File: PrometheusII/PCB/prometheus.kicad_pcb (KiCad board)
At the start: 4 copper layers, 223.5 x 222.3 mm, 203 parts, among them J1 0878311420, J10 Conn_02x02_Odd_Even, J11 Conn_02x02_Odd_Even, J16 Conn_02x07_Odd_Even, J17 Conn_02x07_Odd_Even, J18 Conn_02x07_Odd_Even, J19 Conn_02x07_Odd_Even, J2 Conn_02x08_Odd_Even, J3 Conn_02x02_Odd_Even, J4 Conn_02x02_Odd_Even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

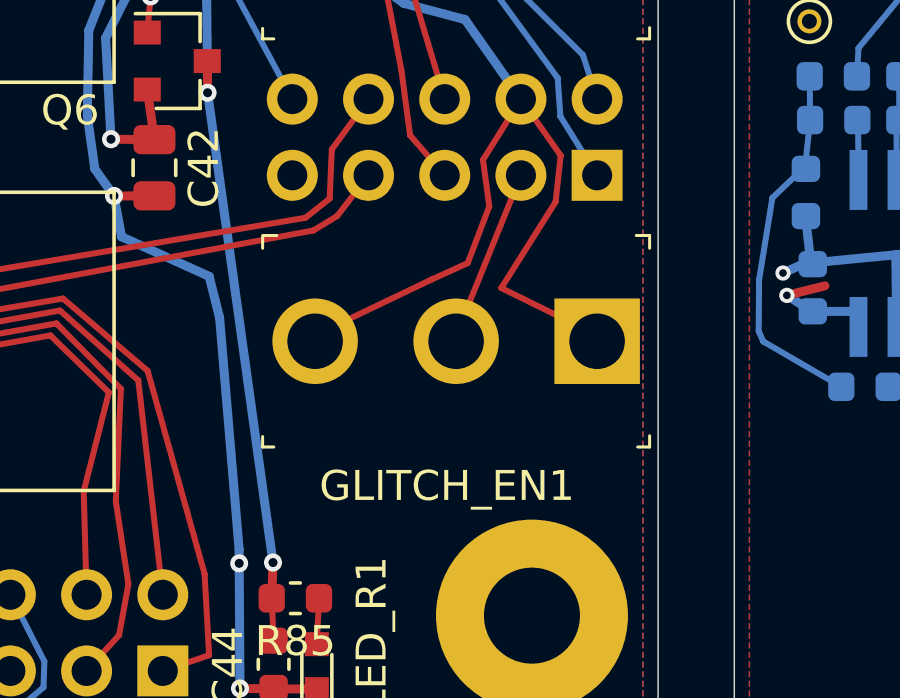
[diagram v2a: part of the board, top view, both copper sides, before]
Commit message: Changed switch PN, keeping footprint the same for now
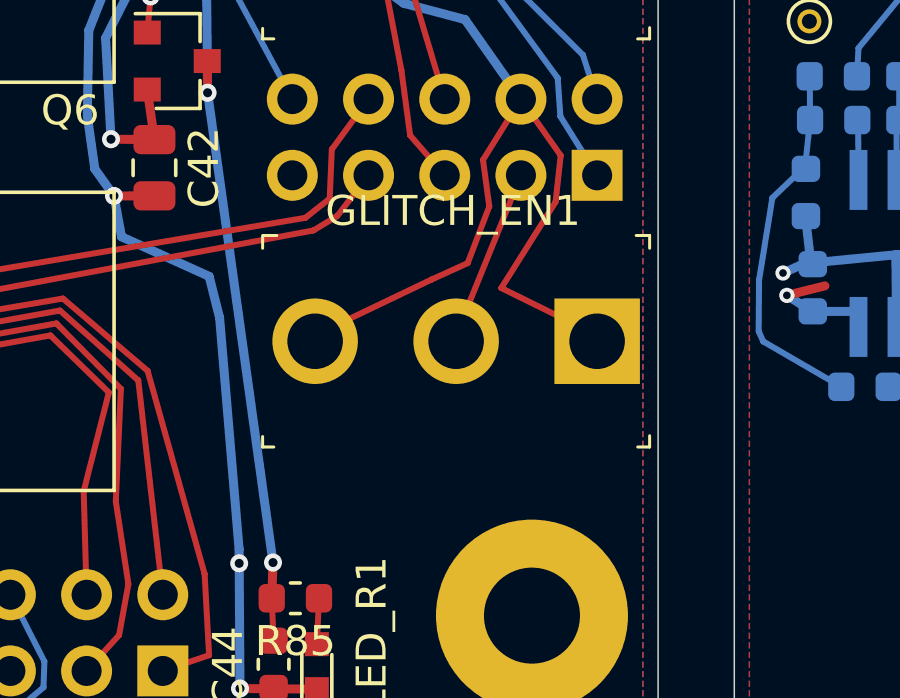
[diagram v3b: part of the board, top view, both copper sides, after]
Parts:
- FREQ_LOCK1, GLITCH_EN1: value 100SP5T1B1M2QEH -> TSM113F1; footprint digikey-footprints:Toggle_Switch_100SP1T1B4M2QE -> ttt_lib:Toggle_Switch_TSM113F1
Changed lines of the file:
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@@
     (add_net "Net-(U9-Pad1)")
   )
+  (module ttt_lib:Toggle_Switch_TSM113F1 locked (layer F.Cu)
+    (at 124.968 116.02 180)
+    (descr http://spec_sheets.e-switch.com/specs/T111597.pdf)
+    (fp_text reference GLITCH_EN1 (at 4.8045 4.34 180) (layer F.SilkS)
+      (effects (font (size 1 1) (thickness 0.15)))
+    )
+    (fp_text value TSM113F1 (at 4.65 4.82 180) (layer F.Fab)
+      (effects (font (size 1 1) (thickness 0.15)))
+    )
+    (fp_circle (center 4.7 0) (end 4.7 3.4) (layer F.Fab) (width 0.1))
+    (fp_line (start 11.3 -3.68) (end 11.3 3.68) (layer F.CrtYd) (width 0.05))
+    (fp_line (start 11.3 3.68) (end -1.9 3.68) (layer F.CrtYd) (width 0.05))
+    (fp_line (start -1.9 3.68) (end -1.9 -3.68) (layer F.CrtYd) (width 0.05))
+    (fp_line (start -1.9 -3.68) (end 11.3 -3.68) (layer F.CrtYd) (width 0.05))
+    (fp_text user %R (at 4.7 0 180) (layer F.Fab)
+      (effects (font (size 1 1) (thickness 0.15)))
+    )
+    (fp_line (start 11.15 3.525) (end 11.15 3.1) (layer F.SilkS) (width 0.1))
+    (fp_line (start 11.125 3.525) (end 10.675 3.525) (layer F.SilkS) (width 0.1))
+    (fp_line (start -1.75 3.525) (end -1.3 3.525) (layer F.SilkS) (width 0.1))
+    (fp_line (start -1.75 3.525) (end -1.75 3.1) (layer F.SilkS) (width 0.1))
+    (fp_line (start -1.75 -3.525) (end -1.75 -3.15) (layer F.SilkS) (width 0.1))
+    (fp_line (start -1.75 -3.525) (end -1.35 -3.525) (layer F.SilkS) (width 0.1))
+    (fp_line (start 10.775 -3.525) (end 11.15 -3.525) (layer F.SilkS) (width 0.1))
+    (fp_line (start 11.15 -3.525) (end 11.15 -3.175) (layer F.SilkS) (width 0.1))
+    (fp_line (start 11.05 3.43) (end 11.05 -3.43) (layer F.Fab) (width 0.1))
+    (fp_line (start -1.65 -3.43) (end -1.65 3.43) (layer F.Fab) (width 0.1))
+    (fp_line (start -1.65 3.43) (end 11.05 3.43) (layer F.Fab) (width 0.1))
+    (fp_line (start -1.65 -3.43) (end 11.05 -3.43) (layer F.Fab) (width 0.1))
+    (pad 1 thru_hole rect (at 0 0 180) (size 2.85 2.85) (drill 1.85) (layers *.Cu *.Mask)
+      (net 1 GND))
+    (pad 2 thru_hole circle (at 4.7 0 180) (size 2.85 2.85) (drill 1.85) (layers *.Cu *.Mask)
+      (net 85 /GLITCH_EN_P))
+    (pad 3 thru_hole circle (at 9.4 0 180) (size 2.85 2.85) (drill 1.85) (layers *.Cu *.Mask)
+      (net 1 GND))
+  )
+  (module ttt_lib:Toggle_Switch_TSM113F1 locked (layer F.Cu)
+    (at 124.968 102.416 180)
+    (descr http://spec_sheets.e-switch.com/specs/T111597.pdf)
+    (fp_text reference FREQ_LOCK1 (at 4.8045 4.34 180) (layer F.SilkS)
+      (effects (font (size 1 1) (thickness 0.15)))
+    )
+    (fp_text value TSM113F1 (at 4.65 4.82 180) (layer F.Fab)
+      (effects (font (size 1 1) (thickness 0.15)))
+    )
+    (fp_circle (center 4.7 0) (end 4.7 3.4) (layer F.Fab) (width 0.1))
+    (fp_line (start 11.3 -3.68) (end 11.3 3.68) (layer F.CrtYd) (width 0.05))
+    (fp_line (start 11.3 3.68) (end -1.9 3.68) (layer F.CrtYd) (width 0.05))
+    (fp_line (start -1.9 3.68) (end -1.9 -3.68) (layer F.CrtYd) (width 0.05))
+    (fp_line (start -1.9 -3.68) (end 11.3 -3.68) (layer F.CrtYd) (width 0.05))
+    (fp_text user %R (at 4.7 0 180) (layer F.Fab)
+      (effects (font (size 1 1) (thickness 0.15)))
+    )
+    (fp_line (start 11.15 3.525) (end 11.15 3.1) (layer F.SilkS) (width 0.1))
+    (fp_line (start 11.125 3.525) (end 10.675 3.525) (layer F.SilkS) (width 0.1))
+    (fp_line (start -1.75 3.525) (end -1.3 3.525) (layer F.SilkS) (width 0.1))
+    (fp_line (start -1.75 3.525) (end -1.75 3.1) (layer F.SilkS) (width 0.1))
+    (fp_line (start -1.75 -3.525) (end -1.75 -3.15) (layer F.SilkS) (width 0.1))
+    (fp_line (start -1.75 -3.525) (end -1.35 -3.525) (layer F.SilkS) (width 0.1))
+    (fp_line (start 10.775 -3.525) (end 11.15 -3.525) (layer F.SilkS) (width 0.1))
+    (fp_line (start 11.15 -3.525) (end 11.15 -3.175) (layer F.SilkS) (width 0.1))
+    (fp_line (start 11.05 3.43) (end 11.05 -3.43) (layer F.Fab) (width 0.1))
+    (fp_line (start -1.65 -3.43) (end -1.65 3.43) (layer F.Fab) (width 0.1))
+    (fp_line (start -1.65 3.43) (end 11.05 3.43) (layer F.Fab) (width 0.1))
+    (fp_line (start -1.65 -3.43) (end 11.05 -3.43) (layer F.Fab) (width 0.1))
+    (pad 1 thru_hole rect (at 0 0 180) (size 2.85 2.85) (drill 1.85) (layers *.Cu *.Mask)
+      (net 1 GND))
+    (pad 2 thru_hole circle (at 4.7 0 180) (size 2.85 2.85) (drill 1.85) (layers *.Cu *.Mask)
+      (net 93 /FREQ_LOCK_P))
+    (pad 3 thru_hole circle (at 9.4 0 180) (size 2.85 2.85) (drill 1.85) (layers *.Cu *.Mask)
+      (net 1 GND))
+  )
   (module ttt_lib:Teensy40_outerpins locked (layer B.Cu)
     (at 190.8302 109.0676 90)
@@
     )
   )
-  (module digikey-footprints:Toggle_Switch_100SP1T1B4M2QE locked (layer F.Cu)
-    (at 124.968 102.416 180)
-    (descr http://spec_sheets.e-switch.com/specs/T111597.pdf)
-    (fp_text reference FREQ_LOCK1 (at 4.8045 4.34) (layer F.SilkS)
-      (effects (font (size 1 1) (thickness 0.15)))
-    )
-    (fp_text value 100SP5T1B1M2QEH (at 4.65 4.82) (layer F.Fab)
-      (effects (font (size 1 1) (thickness 0.15)))
-    )
-    (fp_line (start -1.65 -3.43) (end 11.05 -3.43) (layer F.Fab) (width 0.1))
-    (fp_line (start -1.65 3.43) (end 11.05 3.43) (layer F.Fab) (width 0.1))
-    (fp_line (start -1.65 -3.43) (end -1.65 3.43) (layer F.Fab) (width 0.1))
-    (fp_line (start 11.05 3.43) (end 11.05 -3.43) (layer F.Fab) (width 0.1))
-    (fp_line (start 11.15 -3.525) (end 11.15 -3.175) (layer F.SilkS) (width 0.1))
-    (fp_line (start 10.775 -3.525) (end 11.15 -3.525) (layer F.SilkS) (width 0.1))
-    (fp_line (start -1.75 -3.525) (end -1.35 -3.525) (layer F.SilkS) (width 0.1))
-    (fp_line (start -1.75 -3.525) (end -1.75 -3.15) (layer F.SilkS) (width 0.1))
-    (fp_line (start -1.75 3.525) (end -1.75 3.1) (layer F.SilkS) (width 0.1))
-    (fp_line (start -1.75 3.525) (end -1.3 3.525) (layer F.SilkS) (width 0.1))
-    (fp_line (start 11.125 3.525) (end 10.675 3.525) (layer F.SilkS) (width 0.1))
-    (fp_line (start 11.15 3.525) (end 11.15 3.1) (layer F.SilkS) (width 0.1))
-    (fp_text user %R (at 4.7 0) (layer F.Fab)
-      (effects (font (size 1 1) (thickness 0.15)))
-    )
-    (fp_line (start -1.9 -3.68) (end 11.3 -3.68) (layer F.CrtYd) (width 0.05))
-    (fp_line (start -1.9 3.68) (end -1.9 -3.68) (layer F.CrtYd) (width 0.05))
-    (fp_line (start 11.3 3.68) (end -1.9 3.68) (layer F.CrtYd) (width 0.05))
-    (fp_line (start 11.3 -3.68) (end 11.3 3.68) (layer F.CrtYd) (width 0.05))
-    (fp_circle (center 4.7 0) (end 4.7 3.4) (layer F.Fab) (width 0.1))
-    (pad 3 thru_hole circle (at 9.4 0 180) (size 2.85 2.85) (drill 1.85) (layers *.Cu *.Mask)
-      (net 1 GND))
-    (pad 2 thru_hole circle (at 4.7 0 180) (size 2.85 2.85) (drill 1.85) (layers *.Cu *.Mask)
-      (net 93 /FREQ_LOCK_P))
-    (pad 1 thru_hole rect (at 0 0 180) (size 2.85 2.85) (drill 1.85) (layers *.Cu *.Mask)
-      (net 1 GND))
-  )
-  (module digikey-footprints:Toggle_Switch_100SP1T1B4M2QE locked (layer F.Cu)
-    (at 124.968 116.02 180)
-    (descr http://spec_sheets.e-switch.com/specs/T111597.pdf)
-    (fp_text reference GLITCH_EN1 (at 5.0045 -4.826) (layer F.SilkS)
-      (effects (font (size 1 1) (thickness 0.15)))
-    )
-    (fp_text value 100SP5T1B1M2QEH (at 4.65 4.82) (layer F.Fab)
-      (effects (font (size 1 1) (thickness 0.15)))
-    )
-    (fp_line (start -1.65 -3.43) (end 11.05 -3.43) (layer F.Fab) (width 0.1))
-    (fp_line (start -1.65 3.43) (end 11.05 3.43) (layer F.Fab) (width 0.1))
-    (fp_line (start -1.65 -3.43) (end -1.65 3.43) (layer F.Fab) (width 0.1))
-    (fp_line (start 11.05 3.43) (end 11.05 -3.43) (layer F.Fab) (width 0.1))
-    (fp_line (start 11.15 -3.525) (end 11.15 -3.175) (layer F.SilkS) (width 0.1))
-    (fp_line (start 10.775 -3.525) (end 11.15 -3.525) (layer F.SilkS) (width 0.1))
-    (fp_line (start -1.75 -3.525) (end -1.35 -3.525) (layer F.SilkS) (width 0.1))
-    (fp_line (start -1.75 -3.525) (end -1.75 -3.15) (layer F.SilkS) (width 0.1))
-    (fp_line (start -1.75 3.525) (end -1.75 3.1) (layer F.SilkS) (width 0.1))
-    (fp_line (start -1.75 3.525) (end -1.3 3.525) (layer F.SilkS) (width 0.1))
-    (fp_line (start 11.125 3.525) (end 10.675 3.525) (layer F.SilkS) (width 0.1))
-    (fp_line (start 11.15 3.525) (end 11.15 3.1) (layer F.SilkS) (width 0.1))
-    (fp_text user %R (at 4.7 0) (layer F.Fab)
-      (effects (font (size 1 1) (thickness 0.15)))
-    )
-    (fp_line (start -1.9 -3.68) (end 11.3 -3.68) (layer F.CrtYd) (width 0.05))
-    (fp_line (start -1.9 3.68) (end -1.9 -3.68) (layer F.CrtYd) (width 0.05))
-    (fp_line (start 11.3 3.68) (end -1.9 3.68) (layer F.CrtYd) (width 0.05))
-    (fp_line (start 11.3 -3.68) (end 11.3 3.68) (layer F.CrtYd) (width 0.05))
-    (fp_circle (center 4.7 0) (end 4.7 3.4) (layer F.Fab) (width 0.1))
-    (pad 3 thru_hole circle (at 9.4 0 180) (size 2.85 2.85) (drill 1.85) (layers *.Cu *.Mask)
-      (net 1 GND))
-    (pad 2 thru_hole circle (at 4.7 0 180) (size 2.85 2.85) (drill 1.85) (layers *.Cu *.Mask)
-      (net 85 /GLITCH_EN_P))
-    (pad 1 thru_hole rect (at 0 0 180) (size 2.85 2.85) (drill 1.85) (layers *.Cu *.Mask)
-      (net 1 GND))
-  )
   (module Resistor_SMD:R_0603_1608Metric locked (layer B.Cu)

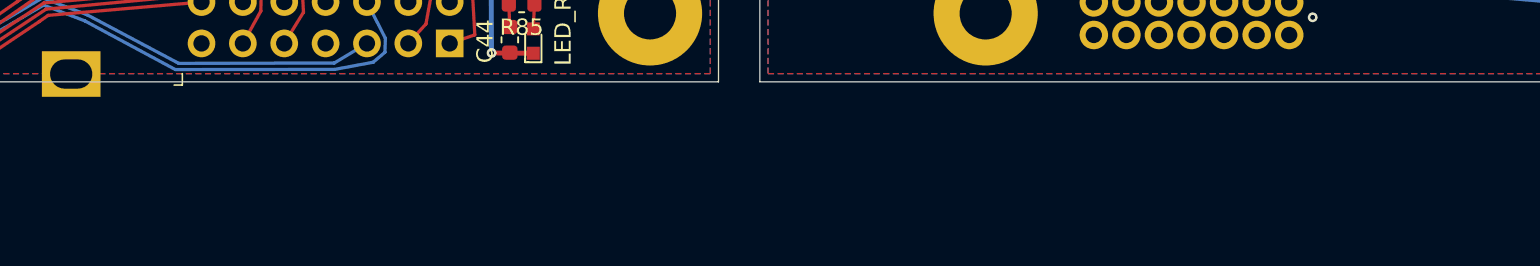
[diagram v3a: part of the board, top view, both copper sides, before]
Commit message: put fiducials in design
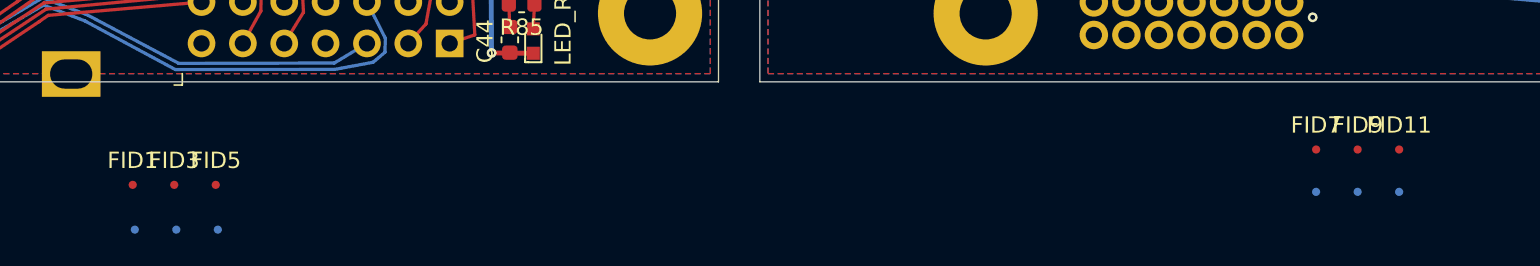
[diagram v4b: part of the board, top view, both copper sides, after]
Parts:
- added FID1: Fiducial, Fiducial:Fiducial_0.5mm_Mask1mm, F.Cu at (91.0, 135.7)
- added FID10: Fiducial, Fiducial:Fiducial_0.5mm_Mask1mm, B.Cu at (166.3, 136.1)
- added FID11: Fiducial, Fiducial:Fiducial_0.5mm_Mask1mm, F.Cu at (168.8, 133.5)
- added FID12: Fiducial, Fiducial:Fiducial_0.5mm_Mask1mm, B.Cu at (168.8, 136.1)
- added FID2: Fiducial, Fiducial:Fiducial_0.5mm_Mask1mm, B.Cu at (91.2, 138.4)
- added FID3: Fiducial, Fiducial:Fiducial_0.5mm_Mask1mm, F.Cu at (93.6, 135.7)
- added FID4: Fiducial, Fiducial:Fiducial_0.5mm_Mask1mm, B.Cu at (93.7, 138.4)
- added FID5: Fiducial, Fiducial:Fiducial_0.5mm_Mask1mm, F.Cu at (96.1, 135.7)
- added FID6: Fiducial, Fiducial:Fiducial_0.5mm_Mask1mm, B.Cu at (96.3, 138.4)
- added FID7: Fiducial, Fiducial:Fiducial_0.5mm_Mask1mm, F.Cu at (163.7, 133.5)
- added FID8: Fiducial, Fiducial:Fiducial_0.5mm_Mask1mm, B.Cu at (163.7, 136.1)
- added FID9: Fiducial, Fiducial:Fiducial_0.5mm_Mask1mm, F.Cu at (166.3, 133.5)

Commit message: Working on connector updates
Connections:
- U1 pad 20: /VOCT_FINE_T -> /FREQ_LOCK_T
- U1 pad 21: /VOCT_ATV_T -> /GLITCH_EN_T
- U1 pad 22: /VOCT_T -> /VOCT_FINE_T
- U1 pad 23: /PARAM_0_CV_T -> /VOCT_ATV_T
- U1 pad 24: /LFO_T -> /VOCT_T
- U1 pad 25: /LEN_CV_T -> /PARAM_0_CV_T
- U1 pad 26: /PARAM_0_T -> /LFO_T
- U1 pad 27: /PARAM_1_T -> /LEN_CV_T
- U1 pad 28: /LEN_KNOB_T -> /PARAM_0_T
- U1 pad 29: /FREQ_LOCK_T -> /PARAM_1_T
- U1 pad 30: /GLITCH_EN_T -> /LEN_KNOB_T

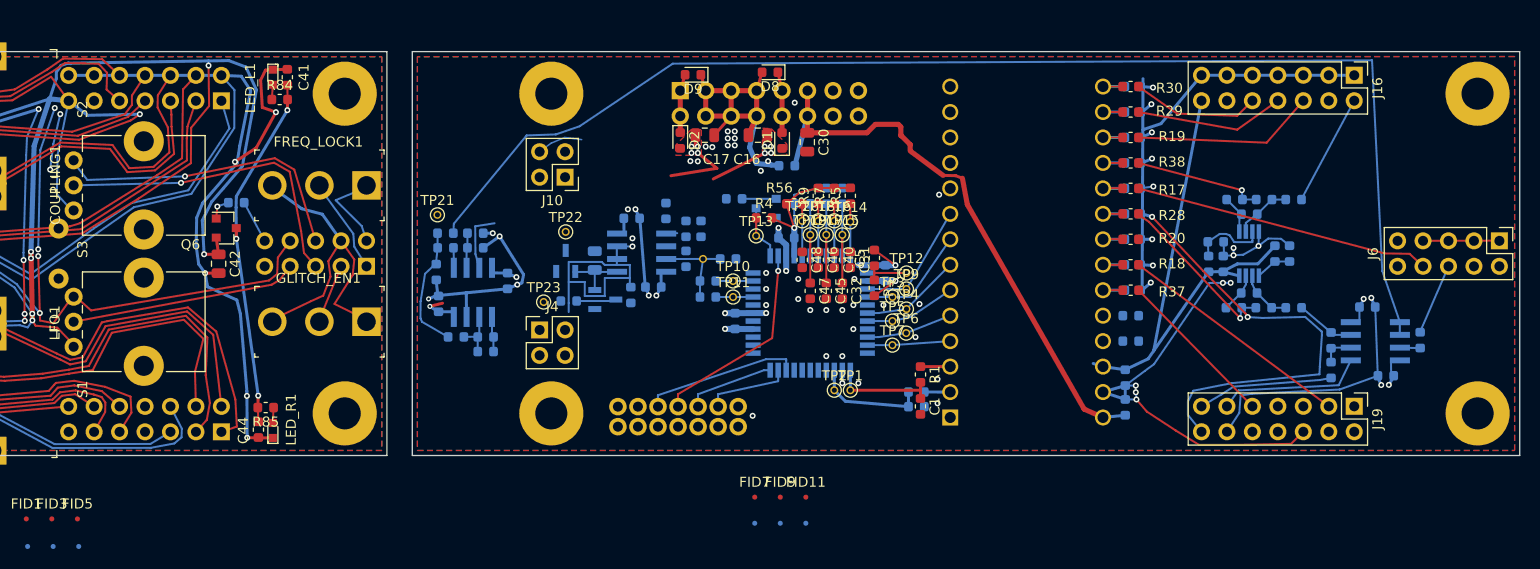
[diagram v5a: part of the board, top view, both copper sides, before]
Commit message: Updated connector placement and footprints
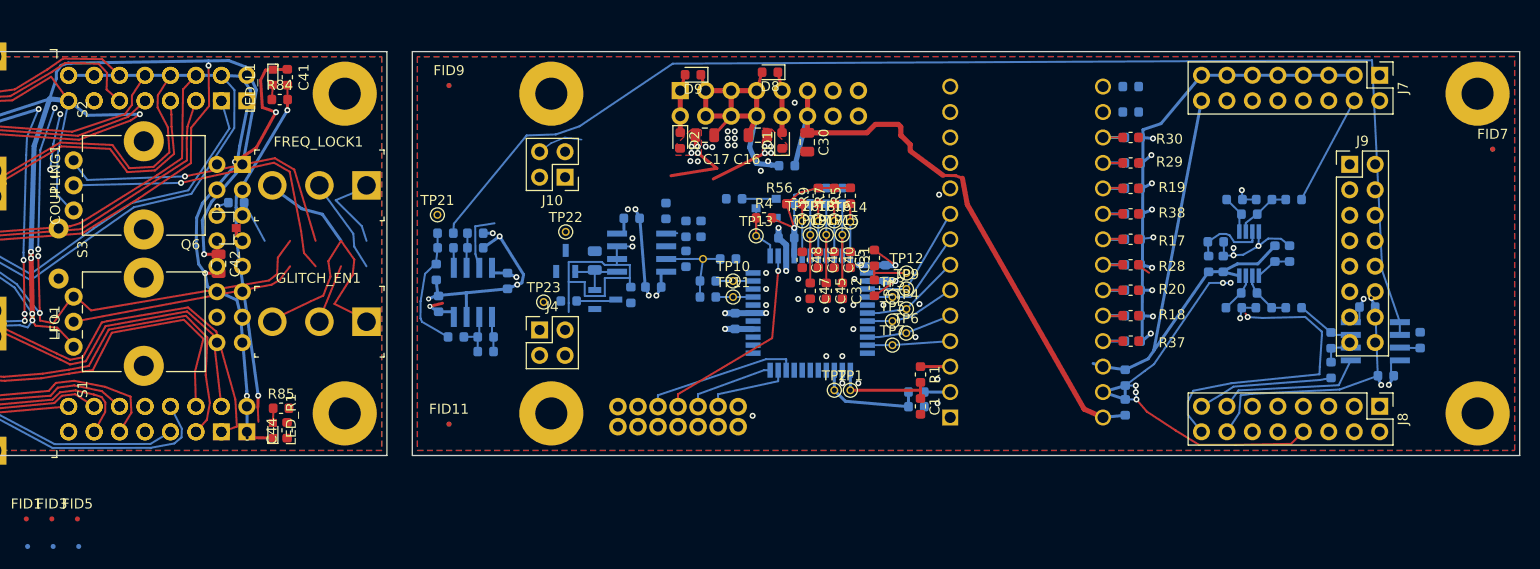
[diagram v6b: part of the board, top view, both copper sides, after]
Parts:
- removed J16, J19: Conn_02x07_Odd_Even, Connector_PinHeader_2.54mm:PinHeader_2x07_P2.54mm_Vertical
- removed J5, J6: Conn_02x05_Odd_Even, Connector_PinHeader_2.54mm:PinHeader_2x05_P2.54mm_Vertical
- added J12: Conn_02x08_Odd_Even, Connector_PinHeader_2.54mm:PinHeader_2x08_P2.54mm_Vertical, B.Cu at (112.6, 100.3)
- added J13: Conn_02x08_Odd_Even, Connector_PinHeader_2.54mm:PinHeader_2x08_P2.54mm_Vertical, B.Cu at (113.0, 94.0)
- added J14: Conn_02x08_Odd_Even, Connector_PinHeader_2.54mm:PinHeader_2x08_P2.54mm_Vertical, B.Cu at (113.0, 127.0)
- added J7: Conn_02x08_Odd_Even, Connector_PinHeader_2.54mm:PinHeader_2x08_P2.54mm_Vertical, F.Cu at (226.1, 91.4)
- added J8: Conn_02x08_Odd_Even, Connector_PinHeader_2.54mm:PinHeader_2x08_P2.54mm_Vertical, F.Cu at (226.1, 124.5)
- added J9: Conn_02x08_Odd_Even, Connector_PinHeader_2.54mm:PinHeader_2x08_P2.54mm_Vertical, F.Cu at (223.1, 100.3)
- moved FID8 82.6 mm to (237.3, 98.8)
- moved FID7 81.4 mm to (237.3, 98.8)
- moved FID10 54.8 mm to (133.2, 92.5)
- moved FID9 52.7 mm to (133.2, 92.5)
- moved FID12 37.0 mm to (133.2, 126.2)
- moved FID11 36.3 mm to (133.2, 126.2)
- moved R52 22.9 mm to (201.2, 92.6)
- moved R59 22.9 mm to (201.2, 95.1)
- moved C21 5.08 mm to (201.4, 97.6)
- moved R30 5.08 mm to (201.2, 97.6)
- moved C11 5.08 mm to (201.4, 107.8)
- moved C12 5.08 mm to (201.4, 115.4)
- moved C13 5.08 mm to (201.4, 102.7)
- moved C14 5.08 mm to (201.4, 112.9)
- moved C19 5.08 mm to (201.4, 110.3)
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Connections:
- net Net-(U1-Pad11) renamed /LED_0_T
- net Net-(U1-Pad12) renamed /LED_1_T
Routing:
- net /LFO: track 29.7 -> 0.00 mm
- net /PARAM_1: track 23.7 -> 0.00 mm
- net GND: track 1321.5 -> 1300.1 mm
- net /VOCT_CV: track 18.4 -> 0.00 mm
- net /LEN_KNOB: track 16.2 -> 0.00 mm
- net /VOCT_ATV: track 15.0 -> 0.00 mm
- net /LEN_CV: track 16.8 -> 3.60 mm
- net /VOCT_FINE: track 12.8 -> 0.00 mm
- net /PARAM_0_CV: track 13.0 -> 2.35 mm
- net /_CV_FILT: track 7.24 -> 0.00 mm

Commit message: Routed output filter, updated bottom side connector pinouts
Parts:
- R22: value 10k -> 100k
- R24: value 100k -> 33k
- moved TP22 5.74 mm to (142.6, 112.4)
- moved R24 3.07 mm to (136.2, 105.6), turned to 180 degrees
- moved C10 1.79 mm to (132.1, 109.3)
- moved C28 1.60 mm to (139.0, 110.4)
- moved C29 1.60 mm to (132.1, 112.6)
- moved U4 1.60 mm to (135.5, 111.5)
- moved R21 1.60 mm to (132.8, 107.0)
- moved R81 1.60 mm to (132.8, 105.6)
- moved C24 1.58 mm to (136.8, 116.0)
- moved R27 1.58 mm to (133.8, 116.0)
- moved R32 1.58 mm to (136.8, 117.4)
- moved TP21 1.55 mm to (132.1, 103.8)
- moved R22 0.37 mm to (136.2, 107.1)
- moved TP23 0.10 mm to (142.6, 114.0)
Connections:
- J10 pad 1: /EXT_CLK_SW -> GND
- J10 pad 2: GND -> /EXT_CLK_SW
- J10 pad 4: GND -> /GLITCH_IN_T
- J11 pad 2: /GLITCH_IN_P -> GND
- J3 pad 1: GND -> /EXT_CLK_P
- J3 pad 2: /EXT_CLK_P -> /GLITCH_IN_P
- J4 pad 1: /GLITCH_IN_T -> GND
- R22 pad 2: +3V3 -> +12V
- R24 pad 1: Net-(R22-Pad1) -> GND
- R24 pad 2: GND -> Net-(R22-Pad1)
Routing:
- net Net-(C23-Pad1): track 0.00 -> 23.2 mm
- net +3V3: track 662.6 -> 647.6 mm, vias 11 -> 10
- net Net-(Q1-Pad3): track 6.15 -> 20.6 mm
- net GND: track 1300.1 -> 1286.1 mm, vias 79 -> 80
- net /OUT: track 25.8 -> 34.9 mm
- net /CV_FILT: track 126.5 -> 118.2 mm
- net Net-(C24-Pad1): track 3.34 -> 10.3 mm
- net /GLITCH_IN_P: track 6.34 -> 0.00 mm
- net /GLITCH_IN_T: track 10.0 -> 14.6 mm
- net Net-(C49-Pad2): track 0.00 -> 4.41 mm
- net +12V: track 80.6 -> 84.3 mm
- net /EXT_CLK_P: track 9.50 -> 6.55 mm
- net Net-(D7-Pad1): track 5.07 -> 2.34 mm
- net Net-(Q2-Pad3): track 3.10 -> 5.15 mm
- net Net-(Q3-Pad1): track 1.78 -> 0.00 mm
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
